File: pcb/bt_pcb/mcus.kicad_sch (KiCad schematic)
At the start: 38 parts, among them IC11 STM32H523CEU6, IC4 STM32H750VBT6, IC5 W25Q512JVEIM, J14 Conn_02x09_Top_Bottom, J15 Conn_JTAG_SWD_10, J2 Conn_JTAG_SWD_10, Y1 Crystal, Y2 Crystal

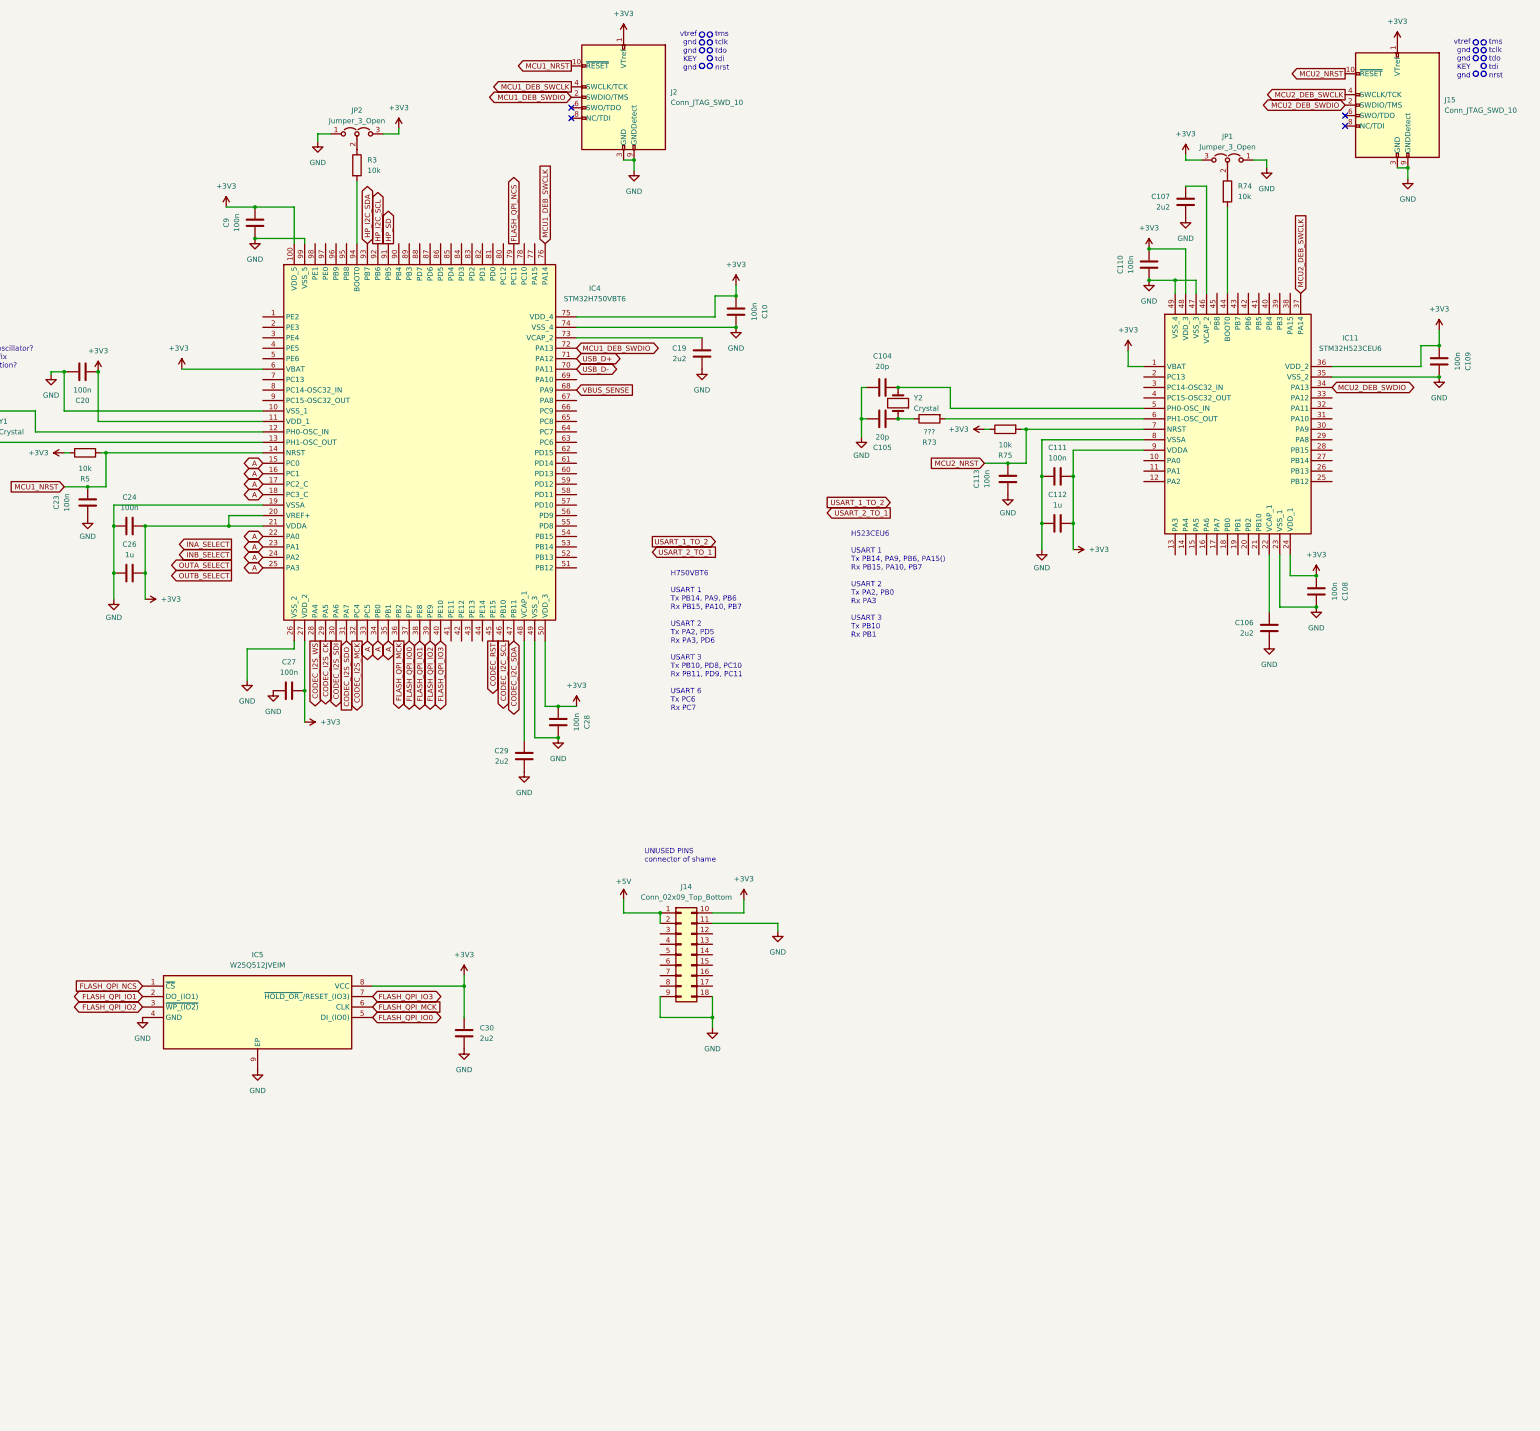
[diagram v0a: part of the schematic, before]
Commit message: ditching power pcb, new codec
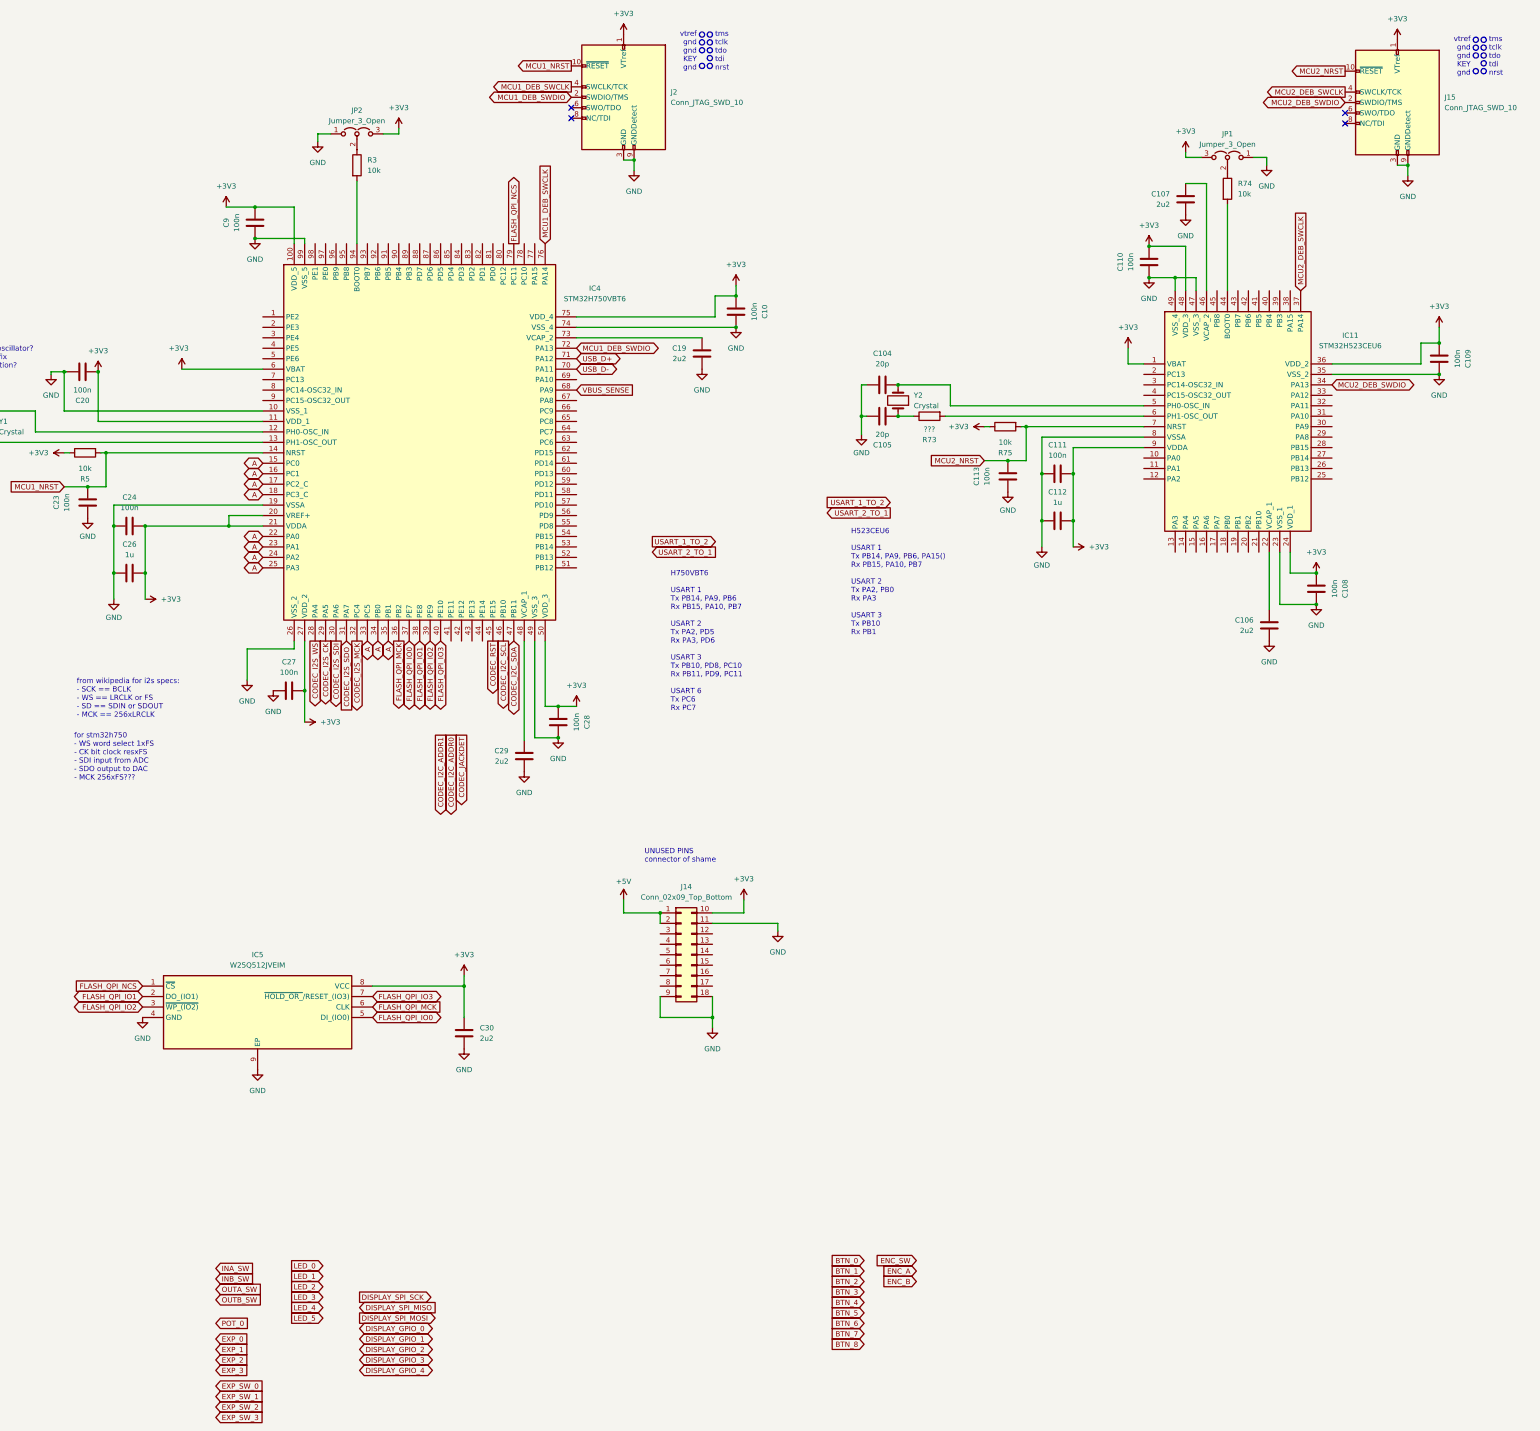
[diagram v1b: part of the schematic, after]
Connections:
- net HP_I2C_SCL: no longer names the net of IC4.92 (PB6)
- net HP_I2C_SDA: no longer names the net of IC4.93 (PB7)
- net HP_SD: no longer names the net of IC4.91 (PB5)
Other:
- note added: "for stm32h750 - WS word select 1xFS - CK bit clock resxFS - SDI input from ADC - SDO output to DAC - MCK 256xFS???"
- note added: "from wikipedia for i2s specs: - SCK == BCLK - WS == LRCLK or FS - SD == SDIN or SDOUT - MCK == 256xLRCLK"
- moved on the sheet: C104, C105, C106, C107, C108, C109, C110, C111, C112, C113, IC11, J15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

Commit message: big progress, now revising error and warnings
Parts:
- removed C104, C105, C21, C22: 20p, symbol Device:C
- removed C113: 100n, symbol Device:C
- removed R73: ???, symbol Device:R
- removed R75: 10k, symbol Device:R
- removed Y1, Y2: Crystal, symbol Device:Crystal
- added C2: 100n, symbol Device:C
- added R13: 10k, symbol Device:R
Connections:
- net CODEC_RST is gone; now on net CODEC_JACKDET: IC4.45 (PE15)
- net +3V3: now also C20.1, R13.1; no longer C20.2
- net CODEC_I2C_ADDR0: now also IC4.44 (PE14)
- net CODEC_I2C_ADDR1: now also IC4.43 (PE13)
- net DISPLAY_GPIO_0: now also IC11.29 (PA8)
- net DISPLAY_GPIO_1: now also IC11.30 (PA9)
- net DISPLAY_GPIO_2: now also IC11.31 (PA10)
- net DISPLAY_GPIO_3: now also IC11.32 (PA11)
- net DISPLAY_GPIO_4: now also IC11.33 (PA12)
- net DISPLAY_SPI_MISO: now also IC11.27 (PB14)
- net DISPLAY_SPI_MOSI: now also IC11.28 (PB15)
- net DISPLAY_SPI_SCK: now also IC11.26 (PB13)
- net ENC_A: now also IC11.3 (PC14-OSC32_IN)
- net ENC_B: now also IC11.4 (PC15-OSC32_OUT)
- net ENC_SW: now also IC11.2 (PC13)
- net EXP_0: now also IC4.22 (PA0)
- net EXP_1: now also IC4.23 (PA1)
- net EXP_2: now also IC4.24 (PA2)
- net EXP_3: now also IC4.25 (PA3)
- net EXP_SW_0: now also IC4.1 (PE2)
- net EXP_SW_1: now also IC4.2 (PE3)
- net EXP_SW_2: now also IC4.3 (PE4)
- net EXP_SW_3: now also IC4.4 (PE5)
- net GND: now also C20.2, C2.1; no longer C20.1
- net INA_SW: now also IC4.54 (PB15)
- net INB_SW: now also IC4.53 (PB14)
- net MCU2_NRST: now also C2.2, R13.2
- net OUTA_SW: now also IC4.52 (PB13)
- net OUTB_SW: now also IC4.51 (PB12)
- net POT_0: now also IC4.18 (PC3_C)
- net USART_1_TO_2: now also IC11.13 (PA3), IC4.63 (PC6)
- net USART_2_TO_1: now also IC11.12 (PA2), IC4.64 (PC7)
- net LED_1_RD: now reaches IC11.25 (PB12)
- net BTN_0_J: now reaches IC11.38 (PA15)
- net BTN_1_J: now reaches IC11.39 (PB3)
- net BTN_2_J: now reaches IC11.40 (PB4)
- net BTN_3_J: now reaches IC11.41 (PB5)
- net BTN_4_J: now reaches IC11.42 (PB6)
- net BTN_8_QB: now reaches IC4.55 (PD8)
- net LED_5_QB: now reaches IC4.56 (PD9)
- net BTN_7_QB: now reaches IC4.57 (PD10)
- net LED_4_QB: now reaches IC4.58 (PD11)
- net BTN_6_QB: now reaches IC4.59 (PD12)
- net LED_3_QB: now reaches IC4.60 (PD13)
- net BTN_5_QB: now reaches IC4.61 (PD14)
- net LED_2_QB: now reaches IC4.62 (PD15)
- net LED_0_RD: now reaches IC4.67 (PA8)
- removed net A: IC4.15 (PC0), IC4.16 (PC1), IC4.17 (PC2_C), IC4.18 (PC3_C), IC4.22 (PA0), IC4.23 (PA1), IC4.24 (PA2), IC4.25 (PA3), IC4.33 (PC5), IC4.34 (PB0), IC4.35 (PB1)
- no-connect marks 4 -> 12
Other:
- note added: "Available analog for H750 PC0, PC1, PC2, PC3, PA0, PA1, PA2, PA3, PC5, PB0, PB1"
- note removed: "which Mhz for the oscillator? and also, how do i fix the clock configuration?"
- moved on the sheet: C20, C23, C27, R5

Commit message: solving some erc warnings and errors
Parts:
- renumbered C23 to C43, C20 to C44, C24 to C45, C26 to C46, C9 to C47, C27 to C48, C30 to C49, C29 to C50, C28 to C51, C19 to C52, C10 to C53, C2 to C54, C111 to C55, C112 to C56, C110 to C57, C107 to C58, C106 to C59, C108 to C60, C109 to C61, IC5 to IC3, IC11 to IC5, J2 to J12, J14 to J13, J15 to J14, JP2 to JP3, JP1 to JP4, R5 to R35, R3 to R36, R13 to R37, R74 to R38
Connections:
- net +5V: no longer J13.2 (Pin_2)
- net GND: now also J13.2 (Pin_2); no longer J13.18 (Pin_18), J13.9 (Pin_9)
- no-connect marks 12 -> 4
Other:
- moved on the sheet: C43, C44, C48, C50, C51, C52, C55, C56, C57, C58, C61, IC3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

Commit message: schematic in theory finished
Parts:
- removed J12, J14: Conn_JTAG_SWD_10, symbol Connector:Conn_ARM_JTAG_SWD_10
- removed J13: Conn_02x09_Top_Bottom, symbol Connector_Generic:Conn_02x09_Top_Bottom
- removed JP3, JP4: Jumper_3_Open, symbol Jumper:Jumper_3_Open
- removed R36, R38: 10k, symbol Device:R
- added J11, J12: FTSH-107-01-L-DV-K-A, library:FTSH-107-XX-YYY-DV-K-A, symbol library:FTSH-107-01-L-DV-K-A
- C43: renamed from C58; value 2u2 -> 2.2u; footprint (none) -> Capacitor_SMD:C_0603_1608Metric_Pad1.08x0.95mm_HandSolder
- C44: renamed from C47; footprint (none) -> Capacitor_SMD:C_0603_1608Metric_Pad1.08x0.95mm_HandSolder
- C45: renamed from C57; footprint (none) -> Capacitor_SMD:C_0603_1608Metric_Pad1.08x0.95mm_HandSolder
- C46: renamed from C53; footprint (none) -> Capacitor_SMD:C_0603_1608Metric_Pad1.08x0.95mm_HandSolder
- C47: renamed from C52; footprint (none) -> Capacitor_SMD:C_0603_1608Metric_Pad1.08x0.95mm_HandSolder
- C48: renamed from C61; footprint (none) -> Capacitor_SMD:C_0603_1608Metric_Pad1.08x0.95mm_HandSolder
- C49: renamed from C44; footprint (none) -> Capacitor_SMD:C_0603_1608Metric_Pad1.08x0.95mm_HandSolder
- C50: renamed from C54; footprint (none) -> Capacitor_SMD:C_0603_1608Metric_Pad1.08x0.95mm_HandSolder
- C51: renamed from C43; footprint (none) -> Capacitor_SMD:C_0603_1608Metric_Pad1.08x0.95mm_HandSolder
- C52: renamed from C55; footprint (none) -> Capacitor_SMD:C_0603_1608Metric_Pad1.08x0.95mm_HandSolder
- C53: renamed from C56; footprint (none) -> Capacitor_SMD:C_0603_1608Metric_Pad1.08x0.95mm_HandSolder
- C54: renamed from C45; footprint (none) -> Capacitor_SMD:C_0603_1608Metric_Pad1.08x0.95mm_HandSolder
- C55: renamed from C46; footprint (none) -> Capacitor_SMD:C_0603_1608Metric_Pad1.08x0.95mm_HandSolder
- C56: renamed from C60; footprint (none) -> Capacitor_SMD:C_0603_1608Metric_Pad1.08x0.95mm_HandSolder
- C57: renamed from C59; footprint (none) -> Capacitor_SMD:C_0603_1608Metric_Pad1.08x0.95mm_HandSolder
- C58: renamed from C51; footprint (none) -> Capacitor_SMD:C_0603_1608Metric_Pad1.08x0.95mm_HandSolder
- C59: renamed from C50; value 2u2 -> 2.2u; footprint (none) -> Capacitor_SMD:C_0603_1608Metric_Pad1.08x0.95mm_HandSolder
- C60: renamed from C48; footprint (none) -> Capacitor_SMD:C_0603_1608Metric_Pad1.08x0.95mm_HandSolder
- C61: renamed from C49; value 2u2 -> 2.2; footprint (none) -> Capacitor_SMD:C_0603_1608Metric_Pad1.08x0.95mm_HandSolder
- R39: renamed from R37; footprint (none) -> Resistor_SMD:R_0603_1608Metric_Pad0.98x0.95mm_HandSolder
- R40: renamed from R35; footprint (none) -> Resistor_SMD:R_0603_1608Metric_Pad0.98x0.95mm_HandSolder
- renumbered IC4 to IC3, IC5 to IC4, IC3 to IC5
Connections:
- net +3V3: now also J11.3, J12.3
- net GND: now also IC3.94 (BOOT0), IC4.44 (BOOT0), J11.11, J11.5, J11.7, J12.11, J12.5, J12.7
- net MCU1_DEB_SWCLK: now also J11.6
- net MCU1_DEB_SWDIO: now also J11.4
- net MCU1_NRST: now also J11.12
- net MCU2_DEB_SWCLK: now also J12.6
- net MCU2_DEB_SWDIO: now also J12.4
- net MCU2_NRST: now also J12.12
- no-connect marks 4 -> 14
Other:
- note added: "STDC14 pinout with ftsh-107-01-l-dv-k-a reserved 1 - 2 reserved T_VCC 3 - 4 T_JTMS/SWDIO GND 5 - 6 T_JCLK/SWCLK GND 7 - 8 T_JTDO/SWO T_JRCLK/NC 9 - 10 T_JTDI/NC GNDDET 11 - 12 T_NRST T_VCP_RX 13 - 14 T_VCP_TX"
- note removed: "UNUSED PINS connector of shame"
- note removed: "tms tclk tdo tdi nrst"
- note removed: "vtref gnd gnd KEY gnd"

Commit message: finished for real, now onto review
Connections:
- net GND: now also IC3.12 (PH0-OSC_IN), IC3.13 (PH1-OSC_OUT), IC3.15 (PC0), IC3.16 (PC1), IC3.17 (PC2_C), IC3.33 (PC5), IC3.34 (PB0), IC3.35 (PB1), IC3.41 (PE11), IC3.42 (PE12), IC3.5 (PE6), IC3.65 (PC8), IC3.66 (PC9), IC3.69 (PA10), IC3.7 (PC13), IC3.77 (PA15), IC3.78 (PC10), IC3.8 (PC14-OSC32_IN), IC3.80 (PC12), IC3.81 (PD0), IC3.82 (PD1), IC3.83 (PD2), IC3.84 (PD3), IC3.85 (PD4), IC3.86 (PD5), IC3.87 (PD6), IC3.88 (PD7), IC3.89 (PB3), IC3.9 (PC15-OSC32_OUT), IC3.90 (PB4), IC3.91 (PB5), IC3.92 (PB6), IC3.93 (PB7), IC3.95 (PB8), IC3.96 (PB9), IC3.97 (PE0), IC3.98 (PE1), IC4.10 (PA0), IC4.11 (PA1), IC4.14 (PA4), IC4.15 (PA5), IC4.16 (PA6), IC4.17 (PA7), IC4.18 (PB0), IC4.19 (PB1), IC4.20 (PB2), IC4.21 (PB10), IC4.43 (PB7), IC4.45 (PB8), IC4.5 (PH0-OSC_IN), IC4.6 (PH1-OSC_OUT)
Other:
- moved on the sheet: C54, C55

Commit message: pcb started
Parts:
- added J15: Conn_01x08, Connector_PinHeader_2.54mm:PinHeader_1x08_P2.54mm_Vertical, symbol Connector_Generic:Conn_01x08
- renumbered J11 to J13, J12 to J14, R39 to R40, R40 to R41
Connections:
- net GND: no longer IC4.14 (PA4), IC4.15 (PA5), IC4.16 (PA6), IC4.17 (PA7), IC4.18 (PB0), IC4.19 (PB1), IC4.20 (PB2), IC4.21 (PB10)
- new net: IC4.14 (PA4), J15.8 (Pin_8)
- new net: IC4.15 (PA5), J15.7 (Pin_7)
- new net: IC4.16 (PA6), J15.6 (Pin_6)
- new net: IC4.17 (PA7), J15.5 (Pin_5)
- new net: IC4.18 (PB0), J15.4 (Pin_4)
- new net: IC4.19 (PB1), J15.3 (Pin_3)
- new net: IC4.20 (PB2), J15.2 (Pin_2)
- new net: IC4.21 (PB10), J15.1 (Pin_1)
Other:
- moved on the sheet: C57

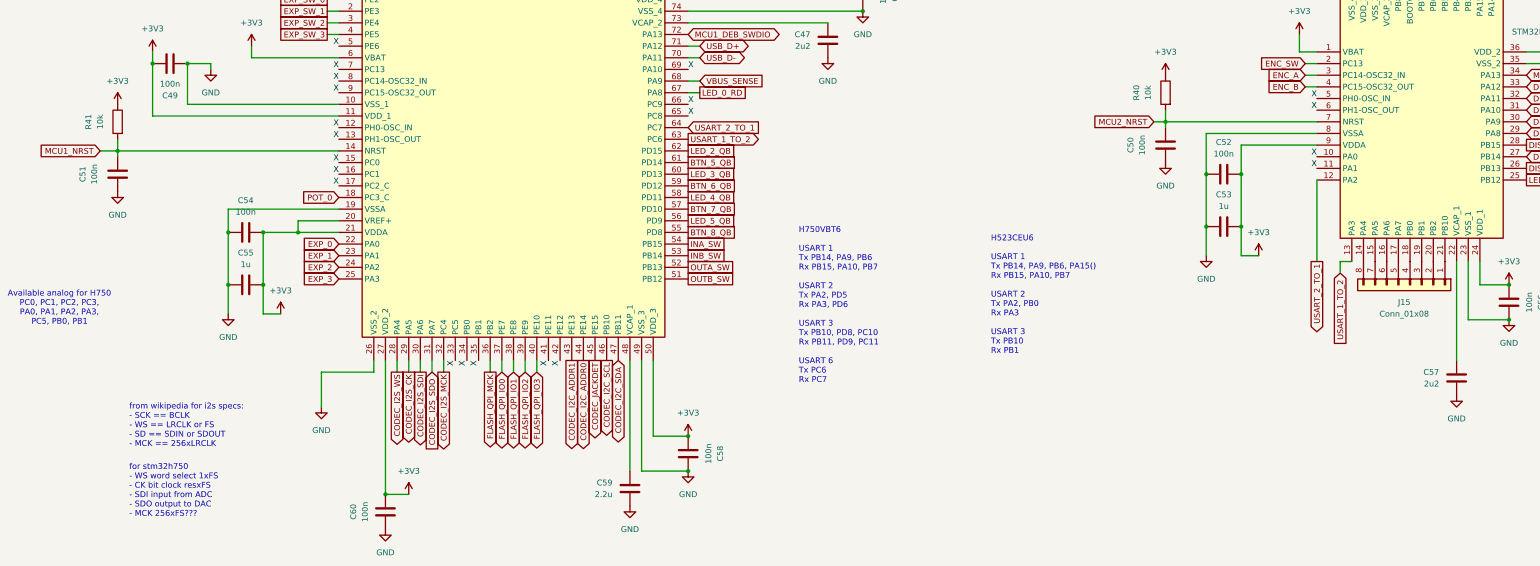
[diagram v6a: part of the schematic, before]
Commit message: pcb with some schematic tuning
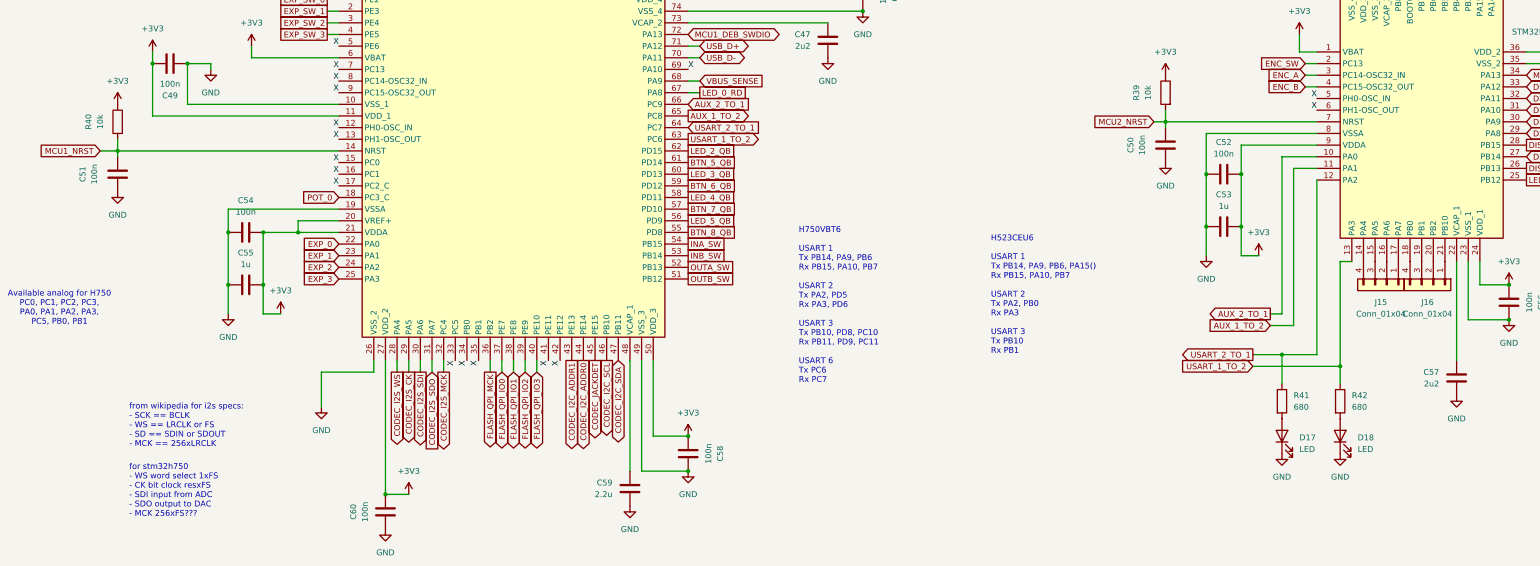
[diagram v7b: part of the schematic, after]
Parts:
- removed J15: Conn_01x08, Connector_PinHeader_2.54mm:PinHeader_1x08_P2.54mm_Vertical, symbol Connector_Generic:Conn_01x08
- added D17, D18: LED, LED_SMD:LED_0603_1608Metric_Pad1.05x0.95mm_HandSolder, symbol Device:LED
- added J15, J16: Conn_01x04, Connector_PinHeader_2.54mm:PinHeader_1x04_P2.54mm_Vertical, symbol Connector_Generic:Conn_01x04
- added R41, R42: 680, Resistor_SMD:R_0603_1608Metric_Pad0.98x0.95mm_HandSolder, symbol Device:R
- renumbered R40 to R39, R41 to R40
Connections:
- net GND: now also D17.1 (K), D18.1 (K); no longer IC3.65 (PC8), IC3.66 (PC9), IC4.10 (PA0), IC4.11 (PA1)
- net USART_1_TO_2: now also R42.1
- net USART_2_TO_1: now also R41.1
- net at IC4.14 (PA4): now also J15.4 (Pin_4)
- net at IC4.15 (PA5): now also J15.3 (Pin_3)
- net at IC4.16 (PA6): now also J15.2 (Pin_2)
- net at IC4.17 (PA7): now also J15.1 (Pin_1)
- net at IC4.18 (PB0): now also J16.4 (Pin_4)
- net at IC4.19 (PB1): now also J16.3 (Pin_3)
- net at IC4.20 (PB2): now also J16.2 (Pin_2)
- net at IC4.21 (PB10): now also J16.1 (Pin_1)
- new net: D18.2 (A), R42.2
- new net: D17.2 (A), R41.2
- new net AUX_1_TO_2: IC3.65 (PC8), IC4.11 (PA1)
- new net AUX_2_TO_1: IC3.66 (PC9), IC4.10 (PA0)
